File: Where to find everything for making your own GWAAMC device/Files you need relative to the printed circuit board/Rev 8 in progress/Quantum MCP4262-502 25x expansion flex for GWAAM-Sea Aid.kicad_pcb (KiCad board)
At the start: 2 copper layers, 96.7 x 23 mm, 26 parts, among them U10 MCP4262-502E/UN, U11 MCP4262-502E/UN, U12 MCP4262-502E/UN, U13 MCP4262-502E/UN, U14 MCP4262-502E/UN, U15 MCP4262-502E/UN, U16 MCP4262-502E/UN, U17 MCP4262-502E/UN, U18 MCP4262-502E/UN, U19 MCP4262-502E/UN, U20 MCP4262-502E/UN, U21 MCP4262-502E/UN, U22 MCP4262-502E/UN, U23 MCP4262-502E/UN, U24 MCP4262-502E/UN, U25 MCP4262-502E/UN, U26 MCP4262-502E/UN, U27 MCP4262-502E/UN, U28 MCP4262-502E/UN, U29 MCP4262-502E/UN, U30 MCP4262-502E/UN, U31 MCP4262-502E/UN, U32 MCP4262-502E/UN, U33 MCP4262-502E/UN, U9 MCP4262-502E/UN

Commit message: Untested while awaiting bare PCB boards....
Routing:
- net /1st_stage_guard_trace: track 365.2 -> 370.7 mm
- net /U8-Pad5: track 300.9 -> 304.8 mm
- net /U8-Pad8: track 330.0 -> 330.8 mm
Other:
- board text added: "RESIST THE TEMPTATION: KEEP UNBENT UNTIL AFTER COMPONENTS ARE PLACED SO BOARD WILL LAY FLAT FOR YOU DURING SOLDERING. During soldering if a bubble develops between Kapton layers, immediately and minimally pierce one Kapton layer to relieve bubble pressure and keep it from enlargening."
- board text added: "This pattern for troubleshooting resistances can be repeated for U10-U33 in the future"

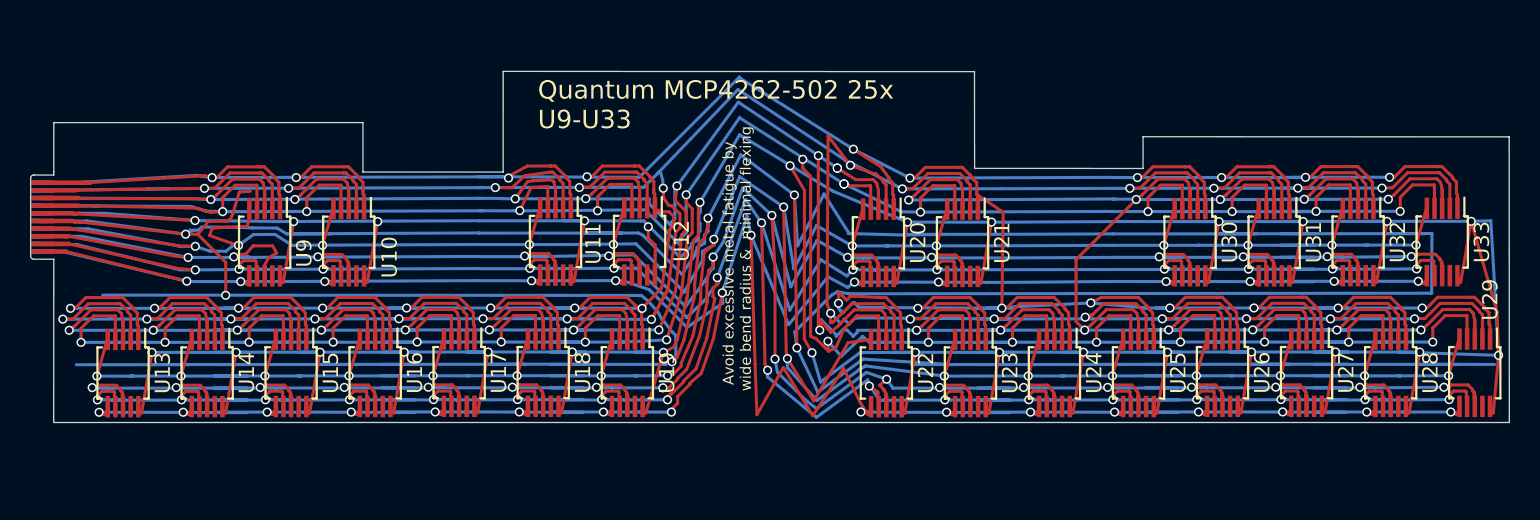
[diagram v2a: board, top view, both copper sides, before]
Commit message: Untested while I'm building it out
These KiCad and zipped gerber files are fully designed but not yet tested while I'm building the bare boards now.  I'm estimating mid- to late-October will see the final evaluation of operation of the entire device.
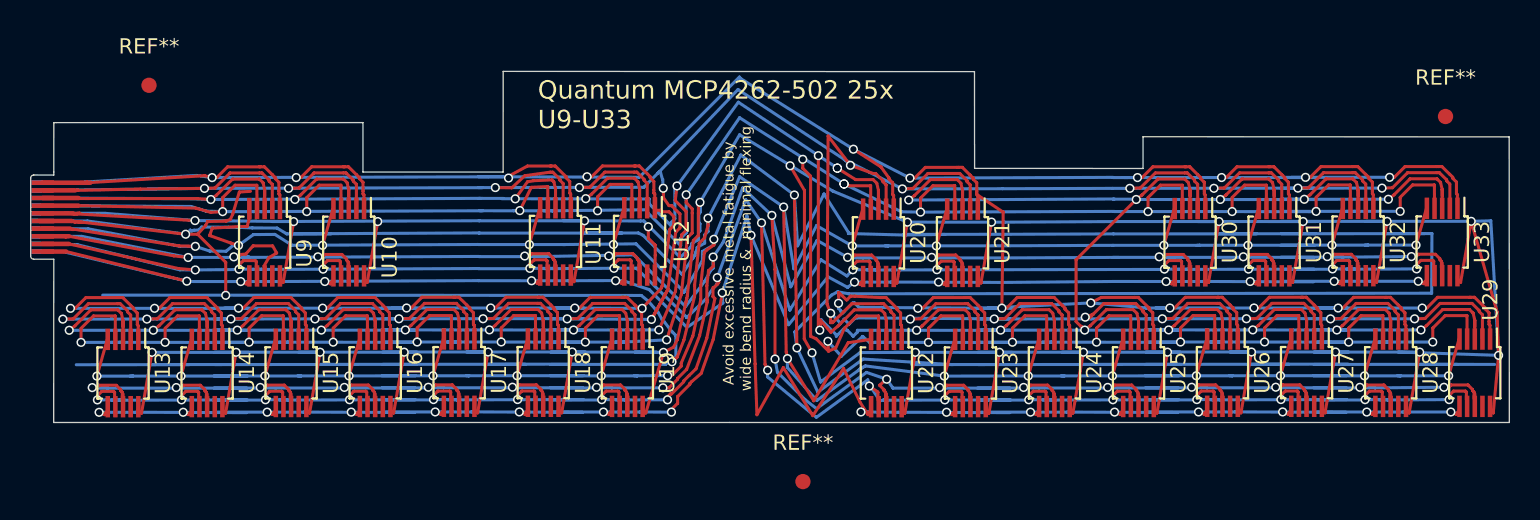
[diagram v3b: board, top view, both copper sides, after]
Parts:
- added REF**: Fiducial_1mm_Mask3mm, Fiducial:Fiducial_1mm_Mask3mm, F.Cu at (163.6, 100.8)
- added REF**: Fiducial_1mm_Mask3mm, Fiducial:Fiducial_1mm_Mask3mm, F.Cu at (78.9, 98.7)
- added REF**: Fiducial_1mm_Mask3mm, Fiducial:Fiducial_1mm_Mask3mm, F.Cu at (121.6, 124.6)
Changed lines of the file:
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@@
     (tracks 2467)
     (zones 0)
-    (modules 26)
+    (modules 29)
     (nets 11)
   )
@@
     (diff_pair_gap 0.25)
   )
+  (module Fiducial:Fiducial_1mm_Mask3mm (layer F.Cu)
+    (at 163.61156 100.77704)
+    (descr "Circular Fiducial, 1mm bare copper, 3mm soldermask opening (recommended)")
+    (tags fiducial)
+    (attr smd)
+    (fp_text reference REF** (at 0 -2.54) (layer F.SilkS)
+      (effects (font (size 1 1) (thickness 0.15)))
+    )
+    (fp_text value Fiducial_1mm_Mask3mm (at 0 2.286) (layer F.Fab)
+      (effects (font (size 1 1) (thickness 0.15)))
+    )
+    (fp_circle (center 0 0) (end 1.75 0) (layer F.CrtYd) (width 0.05))
+    (fp_text user %R (at 0 0) (layer F.Fab)
+      (effects (font (size 0.4 0.4) (thickness 0.06)))
+    )
+    (fp_circle (center 0 0) (end 1.5 0) (layer F.Fab) (width 0.1))
+    (pad "" smd circle (at 0 0) (size 1 1) (layers F.Cu F.Mask)
+      (solder_mask_margin 1) (clearance 1))
+  )
+  (module Fiducial:Fiducial_1mm_Mask3mm (layer F.Cu)
+    (at 78.85938 98.73742)
+    (descr "Circular Fiducial, 1mm bare copper, 3mm soldermask opening (recommended)")
+    (tags fiducial)
+    (attr smd)
+    (fp_text reference REF** (at 0 -2.54) (layer F.SilkS)
+      (effects (font (size 1 1) (thickness 0.15)))
+    )
+    (fp_text value Fiducial_1mm_Mask3mm (at 0 2.286) (layer F.Fab)
+      (effects (font (size 1 1) (thickness 0.15)))
+    )
+    (fp_circle (center 0 0) (end 1.5 0) (layer F.Fab) (width 0.1))
+    (fp_text user %R (at 0 0) (layer F.Fab)
+      (effects (font (size 0.4 0.4) (thickness 0.06)))
+    )
+    (fp_circle (center 0 0) (end 1.75 0) (layer F.CrtYd) (width 0.05))
+    (pad "" smd circle (at 0 0) (size 1 1) (layers F.Cu F.Mask)
+      (solder_mask_margin 1) (clearance 1))
+  )
+  (module Fiducial:Fiducial_1mm_Mask3mm (layer F.Cu)
+    (at 121.60758 124.64288)
+    (descr "Circular Fiducial, 1mm bare copper, 3mm soldermask opening (recommended)")
+    (tags fiducial)
+    (attr smd)
+    (fp_text reference REF** (at 0 -2.54) (layer F.SilkS)
+      (effects (font (size 1 1) (thickness 0.15)))
+    )
+    (fp_text value Fiducial_1mm_Mask3mm (at 0 2.286) (layer F.Fab)
+      (effects (font (size 1 1) (thickness 0.15)))
+    )
+    (fp_circle (center 0 0) (end 1.75 0) (layer F.CrtYd) (width 0.05))
+    (fp_text user %R (at 0 0) (layer F.Fab)
+      (effects (font (size 0.4 0.4) (thickness 0.06)))
+    )
+    (fp_circle (center 0 0) (end 1.5 0) (layer F.Fab) (width 0.1))
+    (pad "" smd circle (at 0 0) (size 1 1) (layers F.Cu F.Mask)
+      (solder_mask_margin 1) (clearance 1))
+  )
   (module multipackage:TE_1-2328702-0_card_edge (layer B.Cu)
